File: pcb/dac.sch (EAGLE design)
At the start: 26 parts, among them Q1 2N7000, U1 PIC16F1773-I/SP, U2 MCP6002-I/P

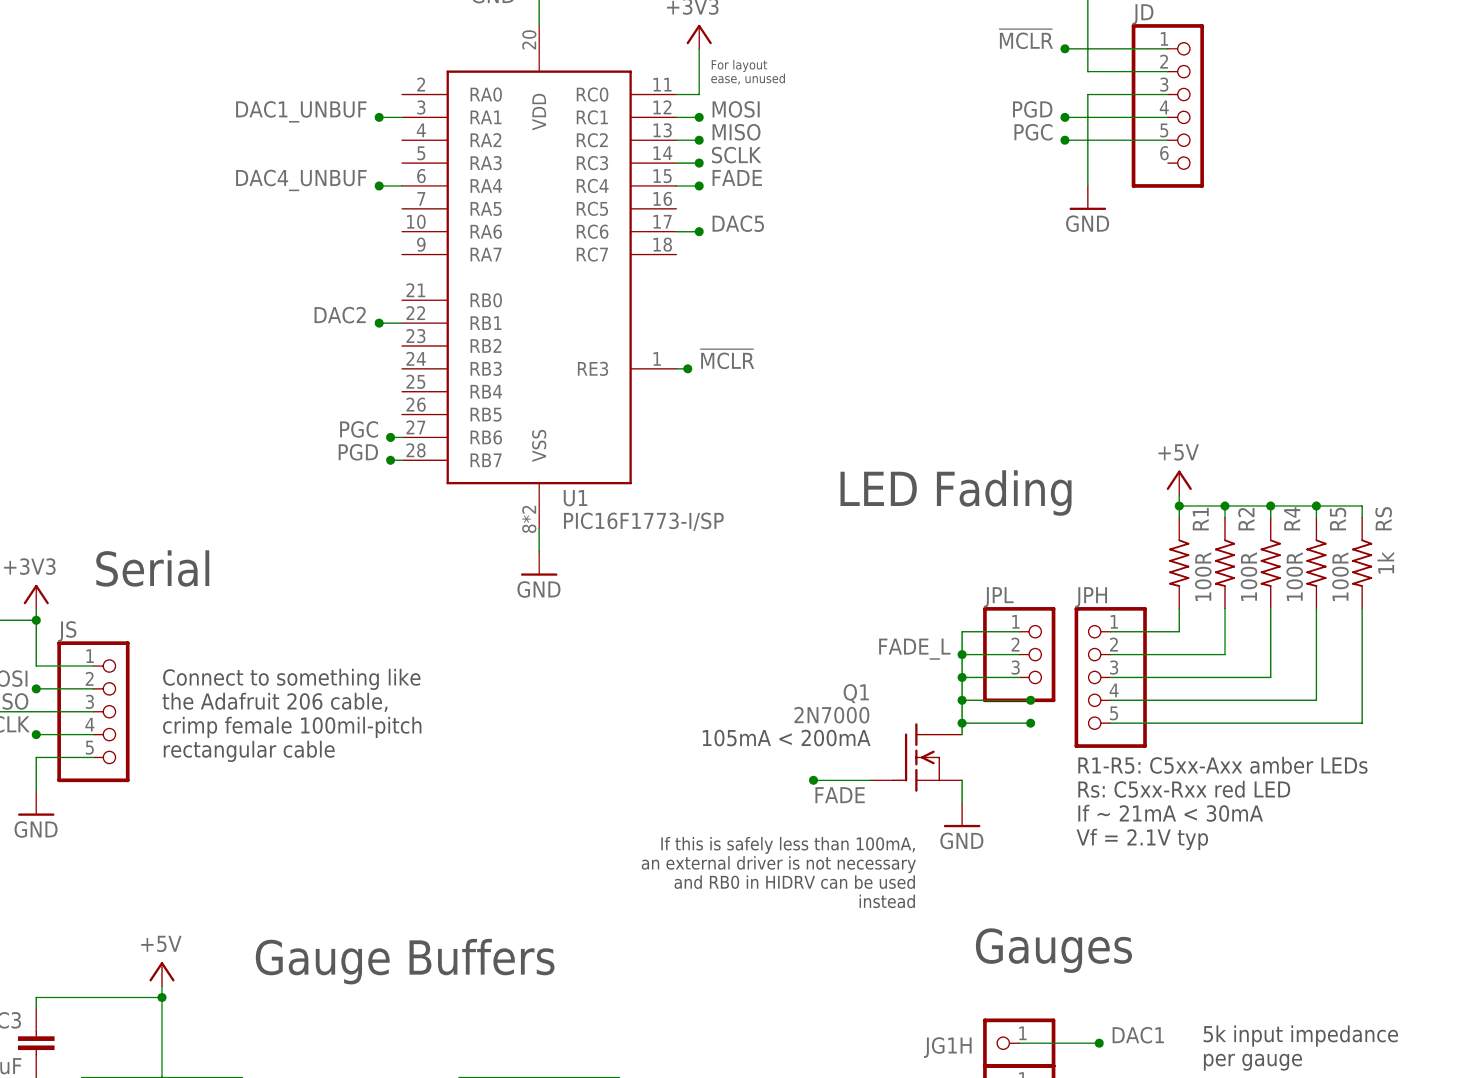
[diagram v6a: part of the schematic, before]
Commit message: Drop FET driver for LEDs; switch to HIDRV on B0 in open-drain mode; LEDs in serial
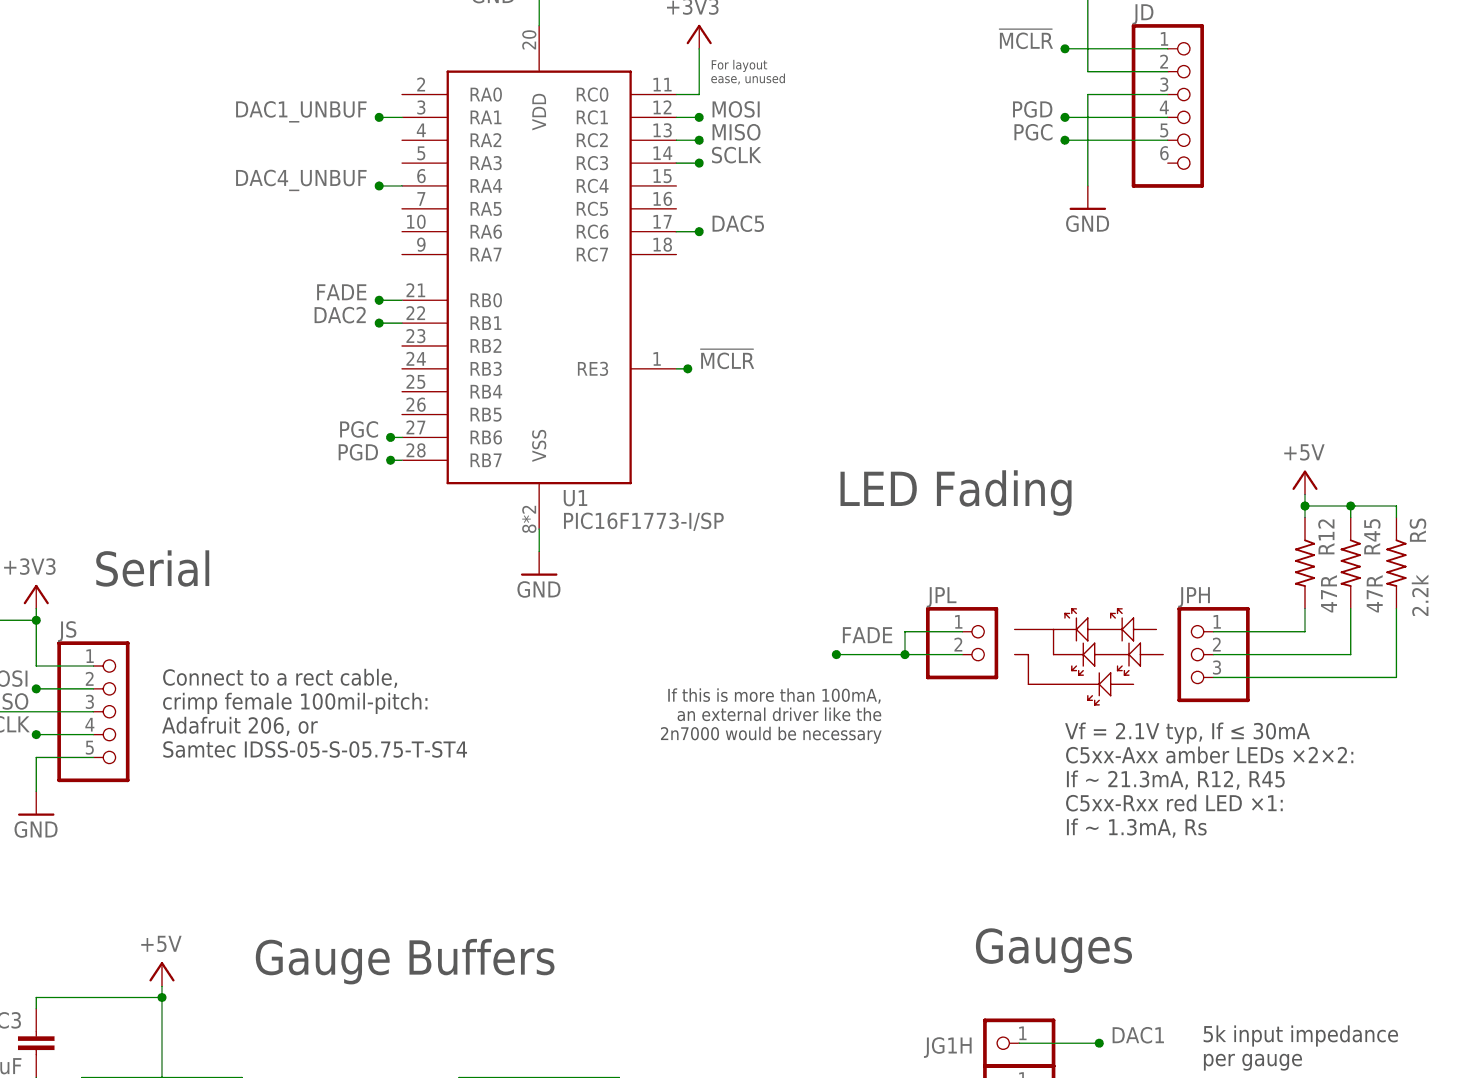
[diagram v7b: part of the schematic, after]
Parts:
- removed Q1: 2N7000, transistor-fet:TN0604N3
- removed R1, R2, R4, R5: 100R, rcl:R-US_0207/2V
- added R12, R45: 47R, rcl:R-US_0207/2V
- JPH: device pinhead:PINHD-1X5 -> pinhead:PINHD-1X3
- JPL: device pinhead:PINHD-1X3 -> pinhead:PINHD-1X2
- RS: value 1k -> 2.2k
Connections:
- removed net FADE_L: JPL.1, JPL.2, JPL.3, Q1.D
- removed net LED4: JPH.3, R4.2
- removed net LED5: JPH.4, R5.2
- net +5V: now also R12.1, R45.1; no longer R1.1, R2.1, R4.1, R5.1
- net FADE: now also JPL.1, JPL.2, U1.RB0; no longer Q1.G, U1.RC4
- net GND: no longer Q1.S
- net LED1: now also R12.2; no longer R1.2
- net LED2: now also R45.2; no longer R2.2
- net LEDSUP: now also JPH.3; no longer JPH.5
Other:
- note added: "Connect to a rect cable, crimp female 100mil-pitch: Adafruit 206, or Samtec IDSS-05-S-05.75-T-ST4"
- note added: "If this is more than 100mA, an external driver like the 2n7000 would be necessary"
- note added: "Vf = 2.1V typ, If ≤ 30mA C5xx-Axx amber LEDs ×2×2: If ~ 21.3mA, R12, R45 C5xx-Rxx red LED ×1: If ~ 1.3mA, Rs"
- note removed: "105mA < 200mA"
- note removed: "Connect to something like the Adafruit 206 cable, crimp female 100mil-pitch rectangular cable"
- note removed: "If this is safely less than 100mA, an external driver is not necessary and RB0 in HIDRV can be used instead"
- note removed: "R1-R5: C5xx-Axx amber LEDs Rs: C5xx-Rxx red LED If ~ 21mA < 30mA Vf = 2.1V typ"
- moved on the sheet: RS

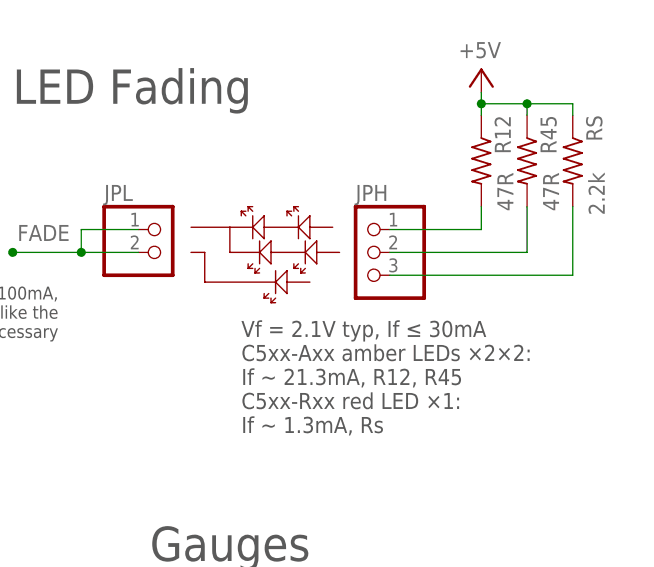
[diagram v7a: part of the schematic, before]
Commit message: Get closer to 30mA based on a parallel approximation; parts on hand and whatnot
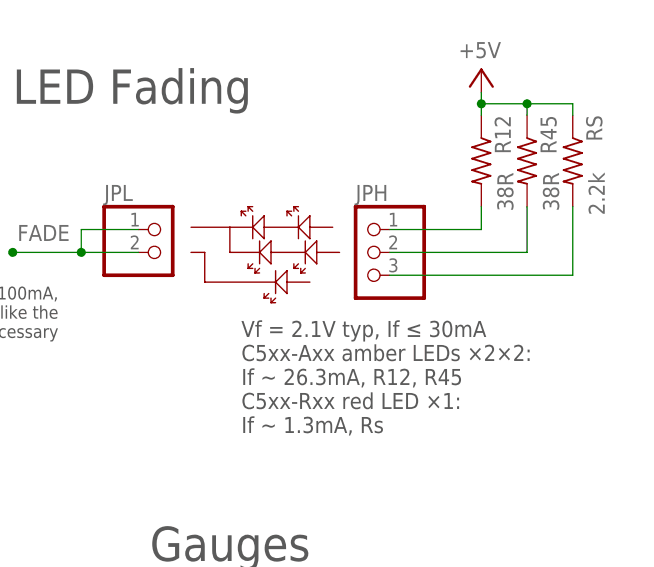
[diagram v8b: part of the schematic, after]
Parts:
- R12, R45: value 47R -> 38R
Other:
- note added: "Vf = 2.1V typ, If ≤ 30mA C5xx-Axx amber LEDs ×2×2: If ~ 26.3mA, R12, R45 C5xx-Rxx red LED ×1: If ~ 1.3mA, Rs"
- note removed: "Vf = 2.1V typ, If ≤ 30mA C5xx-Axx amber LEDs ×2×2: If ~ 21.3mA, R12, R45 C5xx-Rxx red LED ×1: If ~ 1.3mA, Rs"
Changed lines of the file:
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@@
 <part name="GND6" library="supply1" library_urn="urn:adsk.eagle:library:371" deviceset="GND" device=""/>
 <part name="P+4" library="supply1" library_urn="urn:adsk.eagle:library:371" deviceset="+5V" device=""/>
-<part name="R12" library="rcl" library_urn="urn:adsk.eagle:library:334" deviceset="R-US_" device="0207/2V" package3d_urn="urn:adsk.eagle:package:23490/1" value="47R"/>
-<part name="R45" library="rcl" library_urn="urn:adsk.eagle:library:334" deviceset="R-US_" device="0207/2V" package3d_urn="urn:adsk.eagle:package:23490/1" value="47R"/>
+<part name="R12" library="rcl" library_urn="urn:adsk.eagle:library:334" deviceset="R-US_" device="0207/2V" package3d_urn="urn:adsk.eagle:package:23490/1" value="38R"/>
+<part name="R45" library="rcl" library_urn="urn:adsk.eagle:library:334" deviceset="R-US_" device="0207/2V" package3d_urn="urn:adsk.eagle:package:23490/1" value="38R"/>
 <part name="U2" library="linear" library_urn="urn:adsk.eagle:library:262" deviceset="MCP602" device="P" package3d_urn="urn:adsk.eagle:package:16409/2" value="MCP6002-I/P"/>
 <part name="GND8" library="supply1" library_urn="urn:adsk.eagle:library:371" deviceset="GND" device=""/>
@@
 <text x="146.05" y="96.52" size="1.778" layer="97" rot="MR180">Vf = 2.1V typ, If ≤ 30mA
 C5xx-Axx amber LEDs ×2×2:
-If ~ 21.3mA, R12, R45
+If ~ 26.3mA, R12, R45
 C5xx-Rxx red LED ×1:
 If ~ 1.3mA, Rs</text>
